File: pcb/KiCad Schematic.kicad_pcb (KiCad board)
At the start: 2 copper layers, 100 x 100 mm, 70 parts, among them IC1 AP63205WU-7, IC2 ATSAMD51J19A-MU, J1 PAD, J17 Hole, J18 Hole, J19 Hole, J2 Conn_01x02, J20 Hole, J22 Conn_01x06, J3 47346-0001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

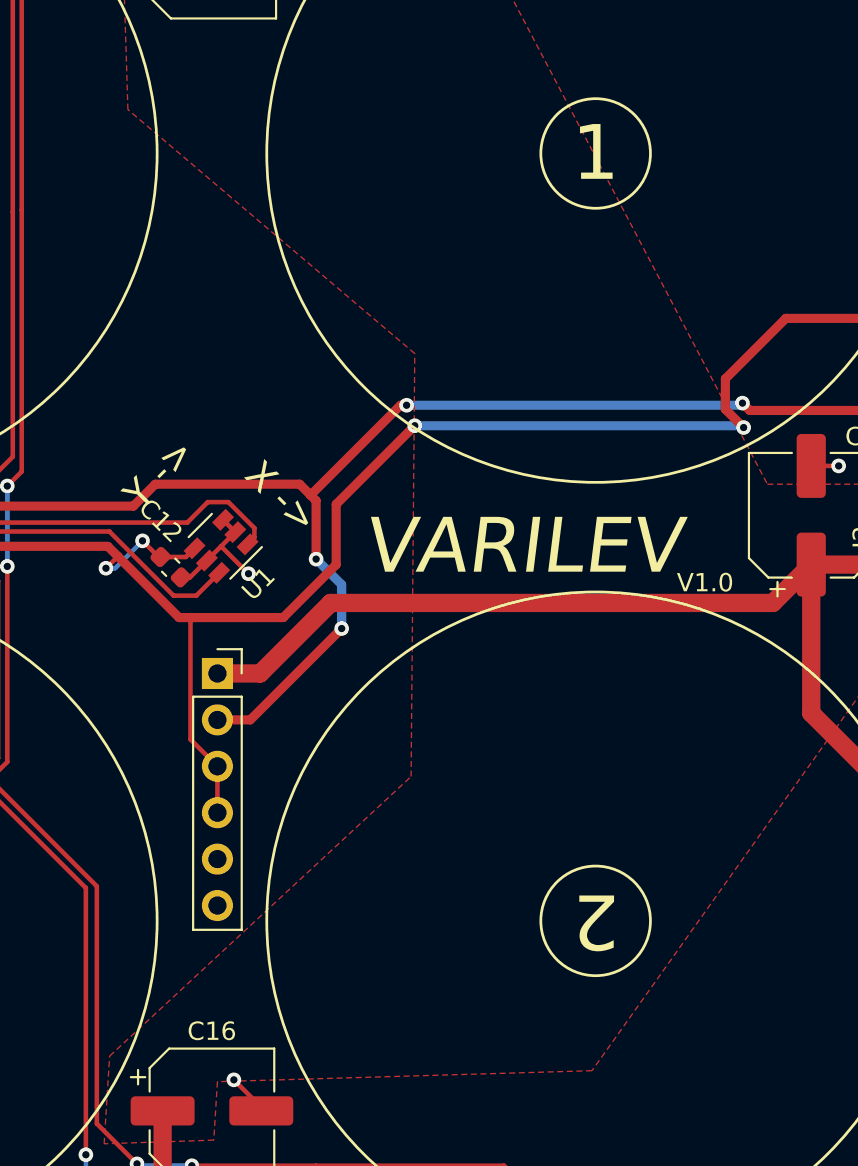
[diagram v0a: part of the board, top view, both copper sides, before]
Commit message: add coil winder hardware, code that compiles (for now)
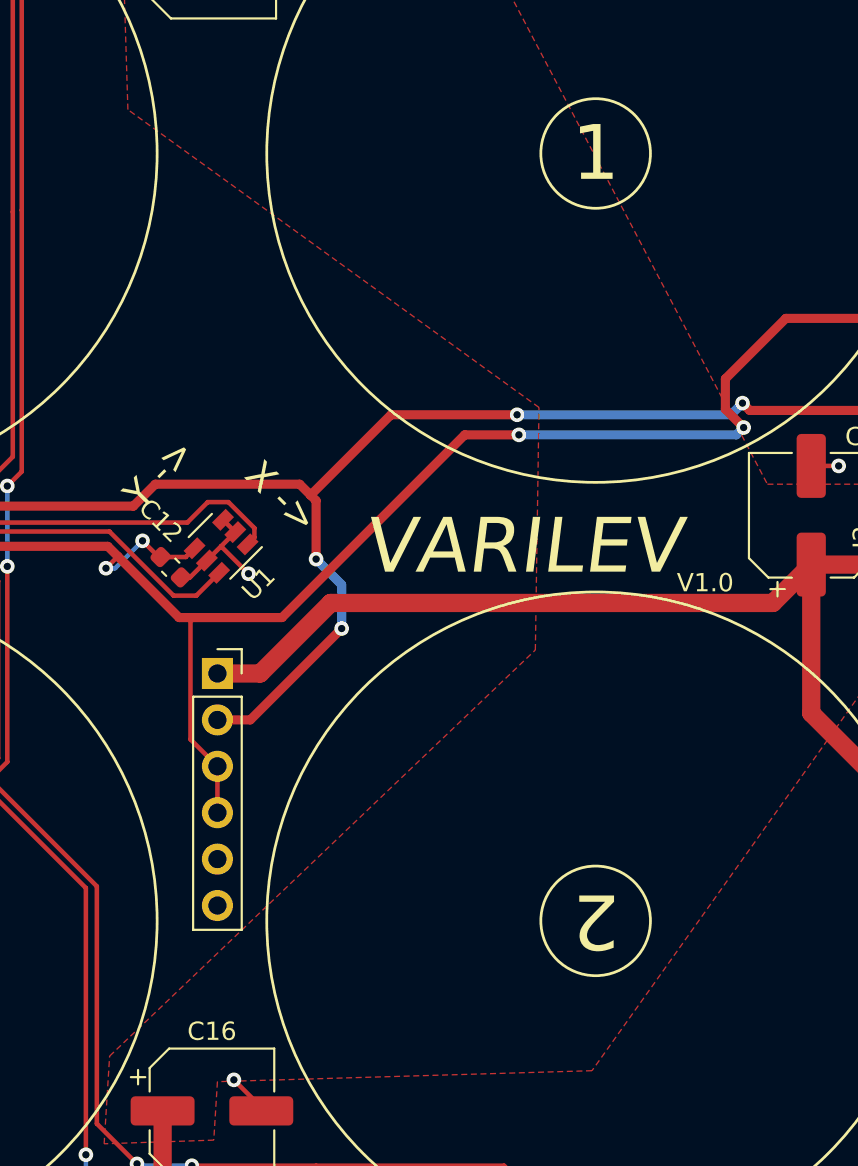
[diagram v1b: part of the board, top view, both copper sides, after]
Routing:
- net +3V3: track 208.3 -> 206.3 mm

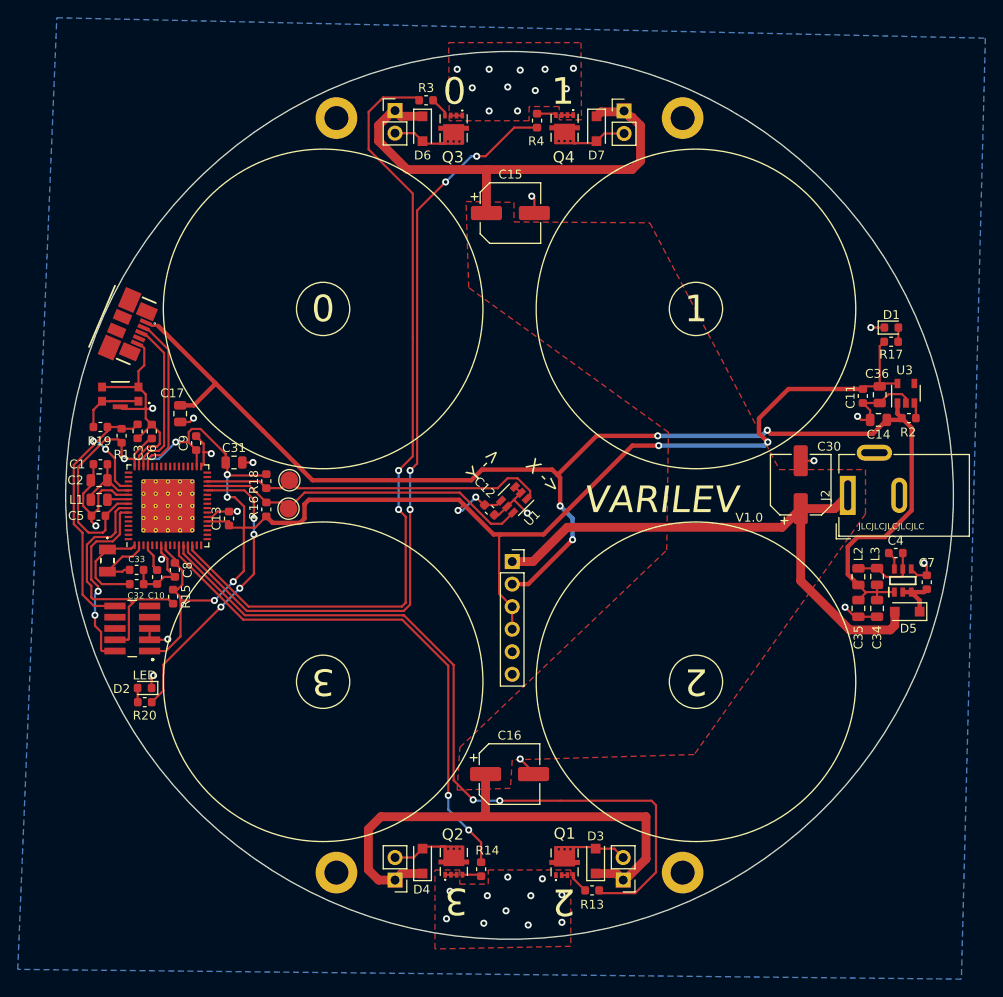
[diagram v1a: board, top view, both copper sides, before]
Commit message: update pcb to use h bridges and other stuff
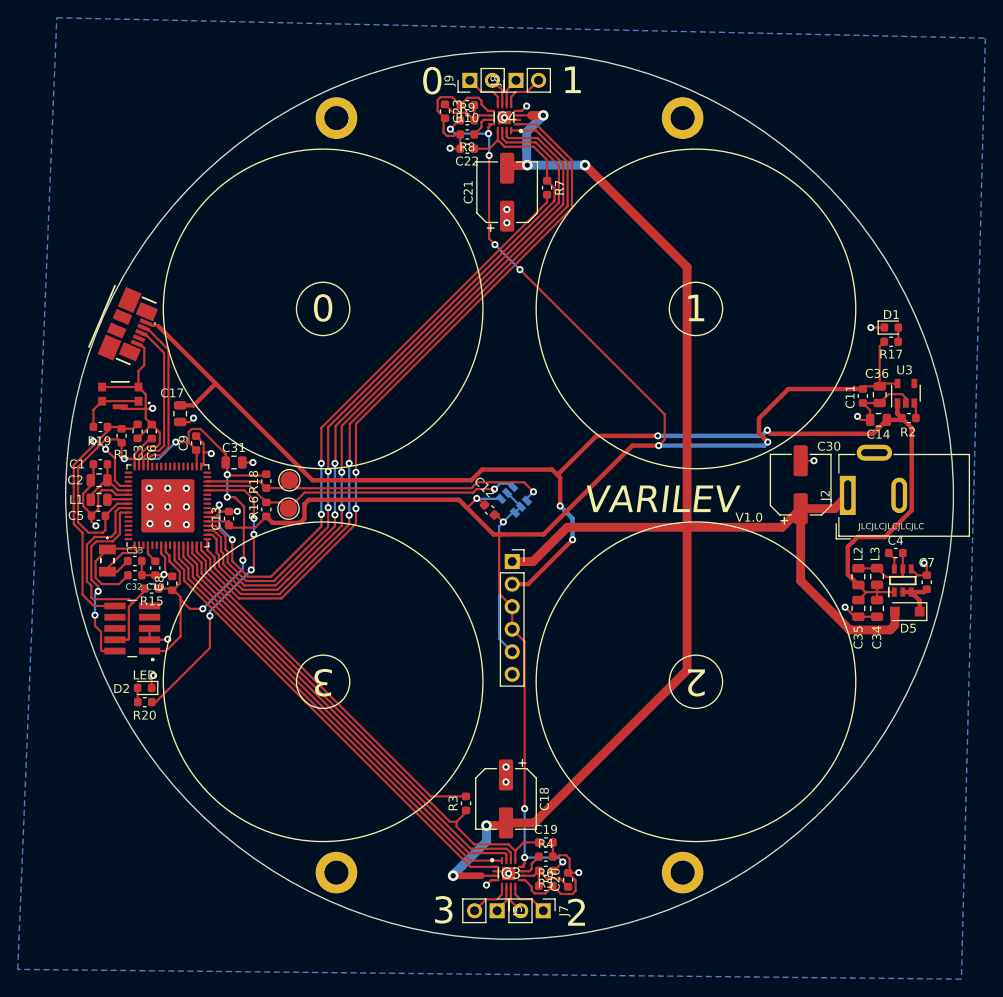
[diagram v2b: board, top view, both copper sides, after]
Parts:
- removed C15, C16: 47uF, Capacitor_SMD:CP_Elec_6.3x7.7
- removed D3, D4, D6, D7: CGRTS4004-HF, Diode_SMD:D_SOD-123F
- removed Q1, Q2, Q3, Q4: NVTFS4C08NTAG, SamacSys_Parts:NVTFS6H854NTAG
- removed R13, R14: 174, Resistor_SMD:R_0603_1608Metric
- added C18: 47uF, Capacitor_SMD:CP_Elec_6.3x7.7, F.Cu at (113.0, 153.4)
- added C19: 22nF, Capacitor_SMD:C_0603_1608Metric, F.Cu at (117.5, 158.3)
- added C20: 100nF, Capacitor_SMD:C_0603_1608Metric, F.Cu at (120.0, 162.5)
- added C21: 47uF, Capacitor_SMD:CP_Elec_6.3x7.7, F.Cu at (113.1, 85.0)
- added C22: 22nF, Capacitor_SMD:C_0603_1608Metric, F.Cu at (108.6, 80.2)
- added C23: 100nF, Capacitor_SMD:C_0603_1608Metric, F.Cu at (106.1, 75.9)
- added IC3: TC78H660FTG,EL, SamacSys_Parts:QFN50P300X300X90-17N, F.Cu at (113.3, 161.8)
- added IC4: TC78H660FTG,EL, SamacSys_Parts:QFN50P300X300X90-17N, F.Cu at (112.8, 76.7)
- added R10: 10k, Resistor_SMD:R_0603_1608Metric, F.Cu at (108.6, 75.2)
- added R5: 10k, Resistor_SMD:R_0603_1608Metric, F.Cu at (117.5, 161.5)
- added R6: 10k, Resistor_SMD:R_0603_1608Metric, F.Cu at (117.5, 163.2)
- added R7: 10k, Resistor_SMD:R_0603_1608Metric, F.Cu at (117.6, 84.5)
- added R8: 75k, Resistor_SMD:R_0603_1608Metric, F.Cu at (108.6, 78.5)
- added R9: 10k, Resistor_SMD:R_0603_1608Metric, F.Cu at (108.6, 77.0)
- IC2: footprint Package_DFN_QFN:QFN-64-1EP_9x9mm_P0.5mm_EP6x6mm_ThermalVias -> Package_DFN_QFN:QFN-64-1EP_9x9mm_P0.5mm_EP6x6mm
- R3: value 174 -> 10k
- R4: value 174 -> 75k
- U1: moved to B.Cu
- moved J8 91.1 mm to (114.1, 72.5), turned to 90 degrees
- moved J5 90.9 mm to (112.0, 166.0), turned to 270 degrees
- moved R4 82.9 mm to (117.5, 159.9), turned to 0 degrees
- moved R3 79.3 mm to (108.5, 153.9), turned to 90 degrees
- moved J9 17.7 mm to (108.9, 72.5), turned to 90 degrees
- moved J7 9.64 mm to (117.2, 166.0), turned to 270 degrees
- moved R15 2.58 mm to (73.1, 129.7), turned to 180 degrees
- moved C8 1.54 mm to (75.4, 129.1), turned to 90 degrees
- moved C10 1.02 mm to (73.5, 127.4)
- moved C32 1.02 mm to (71.2, 128.2)
- moved C33 1.02 mm to (71.2, 126.6)
- turned U1 to 135 degrees
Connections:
- J5 pad 1: +VDC -> Net-(IC3-Pad6)
- J7 pad 1: +VDC -> Net-(IC3-Pad8)
- J8 pad 1: +VDC -> Net-(IC4-Pad6)
- J9 pad 1: +VDC -> Net-(IC4-Pad8)
- R3 pad 1: Net-(Q3-Pad4) -> /GEN4
- R3 pad 2: /GEN4 -> /GEN5
- R4 pad 2: /GEN3 -> GND
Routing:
- net +3V3: track 206.3 -> 291.0 mm, vias 10 -> 17
- net /GEN8: track 0.00 -> 83.4 mm, vias 0 -> 2
- net /GEN6: track 0.00 -> 83.3 mm, vias 0 -> 2
- net /GATE0: track 0.00 -> 82.1 mm, vias 0 -> 2
- net /GATE1: track 0.00 -> 81.8 mm, vias 0 -> 2
- net /GEN7: track 0.00 -> 80.9 mm, vias 0 -> 2
- net /GEN9: track 0.00 -> 69.7 mm, vias 0 -> 4
- net /GEN0: track 0.00 -> 52.9 mm
- net GND: track 104.5 -> 148.3 mm, vias 39 -> 34
- net /GEN5: track 0.00 -> 43.2 mm
- net /GEN3: track 90.9 -> 53.0 mm, vias 4 -> 0
- net /GEN2: track 88.6 -> 53.0 mm, vias 2 -> 0
- net /GEN4: track 92.2 -> 58.1 mm, vias 2 -> 0
- net +VDC: track 177.4 -> 185.5 mm, vias 0 -> 5
- net Net-(C20-Pad1): track 0.00 -> 7.92 mm
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- removed copper zone on F.Cu, net +VDC
- removed copper zone on F.Cu, net GND
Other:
- board text added: "yeeeeeee"
- board text removed: ""Two wrong's don't make a right. But three left's do." - Ma"
- board text removed: "X ->"
- board text removed: "Y ->"

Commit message: firmware stable but not fully working
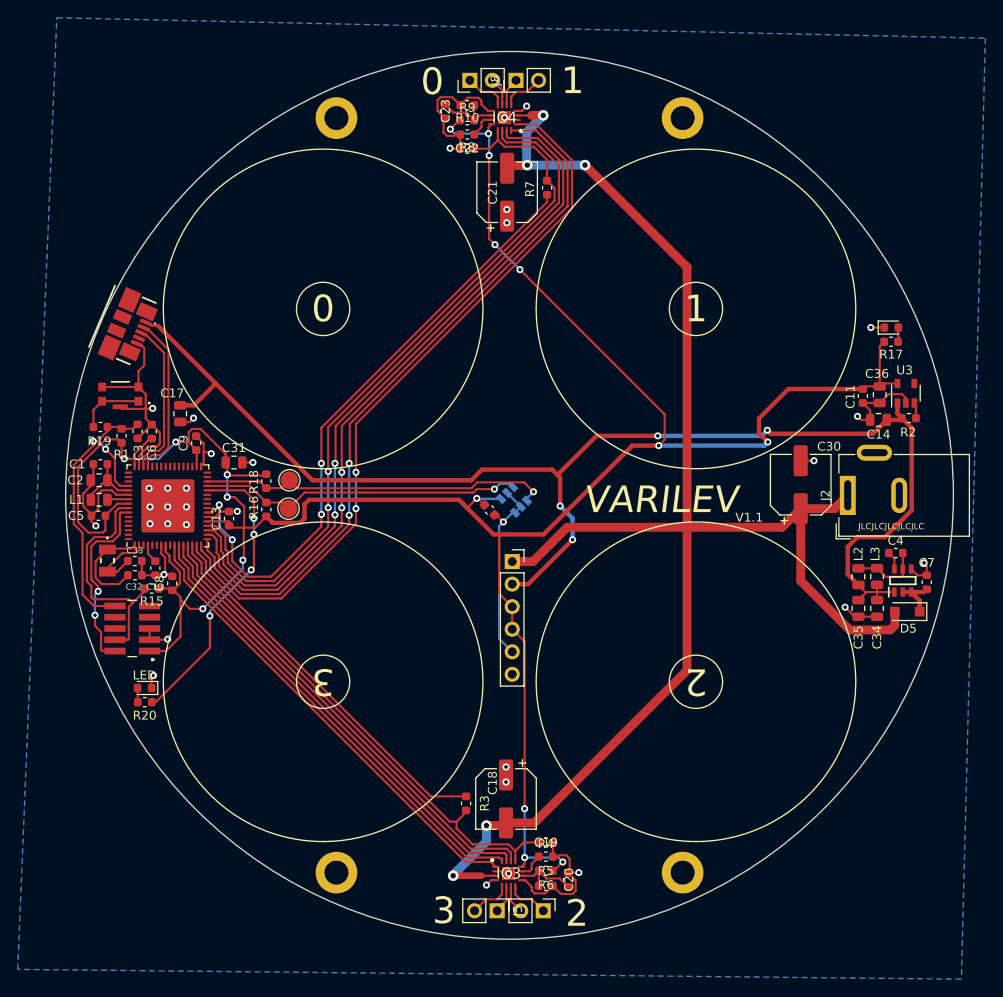
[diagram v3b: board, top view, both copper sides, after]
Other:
- board text added: "V1.1"
- board text removed: "V1.0"
